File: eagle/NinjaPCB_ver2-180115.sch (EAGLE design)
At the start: 78 parts, among them IC2 VNH3SP30-BNC, IC3 ANALOGSW_AD_SOT23-6NC, IC4 ANALOGSW_TI-SC70-5/6NC, IC5 MCP3551SNNC, IC6 NAU7802NC, J2 ATX24, J3 HEATER, J4 HEATER_TEMP, J5 PELTIER, Q2 IRF520NPBF, Q3 IRF520NPBF, U1 CJT1117-3.3-SOT223

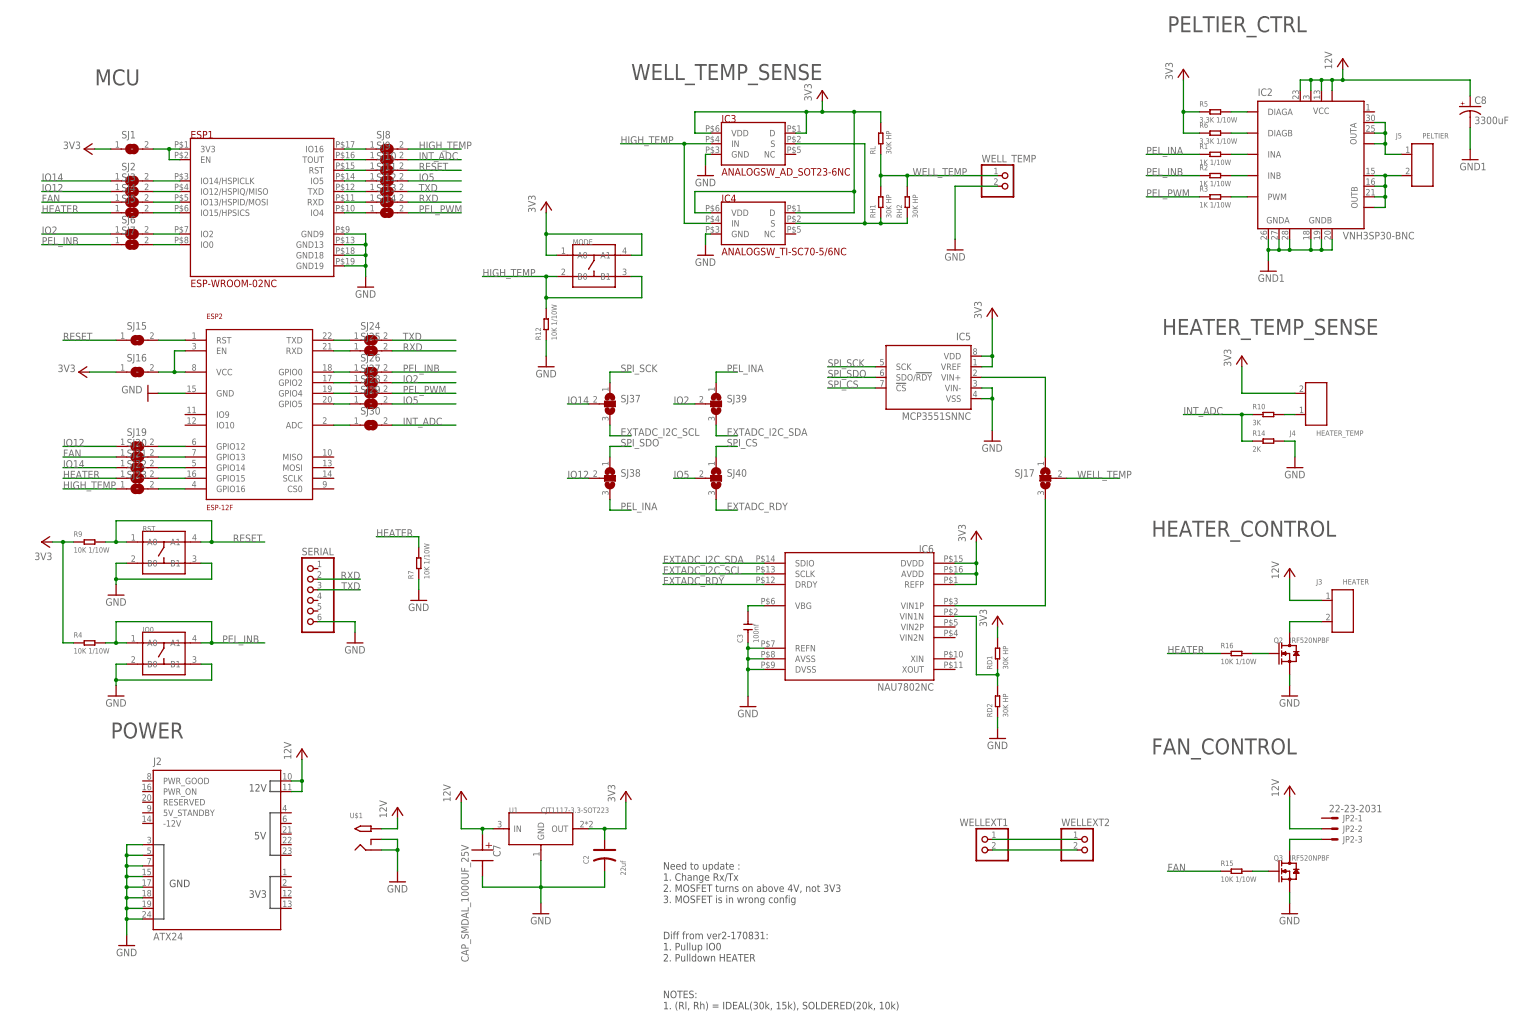
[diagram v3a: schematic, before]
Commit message: use relay instead of driver
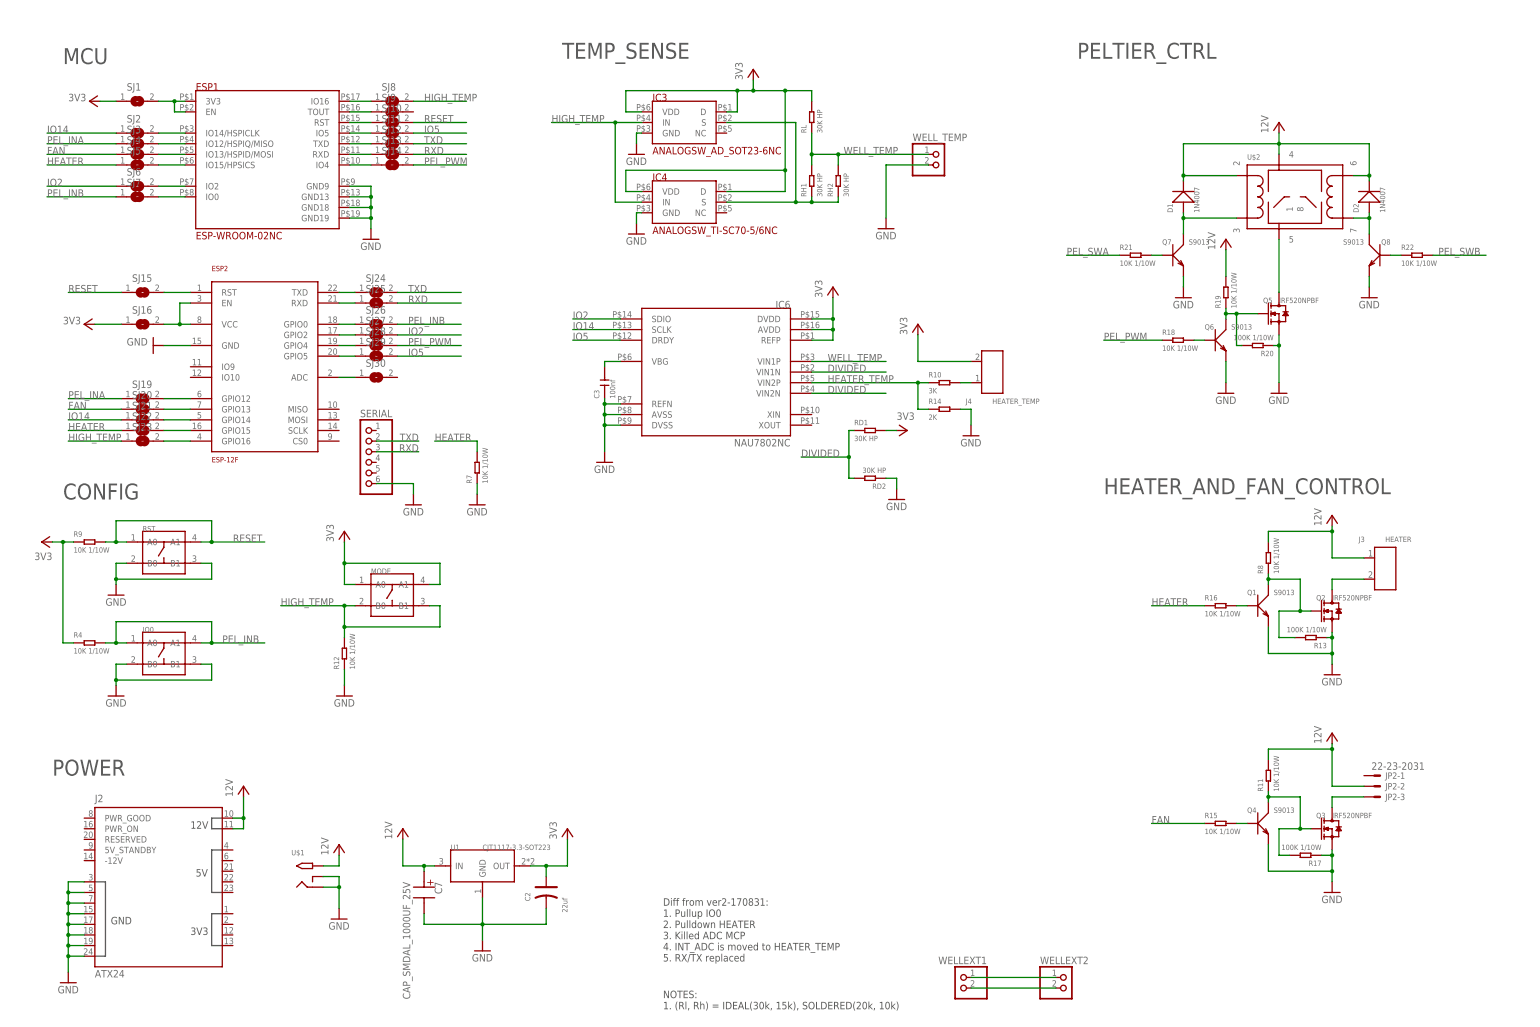
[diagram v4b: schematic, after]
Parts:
- removed C8: 3300uF, PCR-RCL:CAP_E5-13-L3030RINV
- removed IC2: VNH3SP30-BNC, st-microelectronics:VNH3SP30-BNC
- removed IC5: MCP3551SNNC, microchip:MCP3551SNNC
- removed J5: PELTIER, Seeed-Connector:SCREW-TERMINAL-GREEN(2P-3.5)
- removed R1, R2, R3: 1K 1/10W, Seeed-Resistor:SMD-RES-1K-5%-1/10W(0603)
- removed R5, R6: 3.3K 1/10W, Seeed-Resistor:SMD-RES-3.3K-5%-1/10W(0603)
- removed SJ17, SJ37, SJ38, SJ39, SJ40: (no value), jumper:SJ2W
- added D1, D2: 1N4007, Seeed-Diode:DIODE-GEN-PURPOSE-1KV-1A(DO-214AC)
- added Q1, Q4, Q6, Q7, Q8: S9013, Seeed-Transistor:SMD-TRANSISTORS-NPN-25V-500MA-S9013(SOT-23)
- added Q5: IRF520NPBF, Seeed-Transistor:DIP-MOSFET-N-CH-100V-9.7A-IRF520NPBF(TO-220AB)CORRECT
- added R11, R18, R19, R21, R22, R8: 10K 1/10W, Seeed-Resistor:SMD-RES-10K-5%-1/10W(0603)
- added R13, R17, R20: 100K 1/10W, Seeed-Resistor:SMD-RES-100K-5%-1/10W(0603)
- added U$2: NEC-RELAY2ET2, PCR-Switch:NEC-RELAY2ET2
- Q2, Q3: device Seeed-Transistor:DIP-MOSFET-N-CH-100V-9.7A-IRF520NPBF(TO-220AB) -> Seeed-Transistor:DIP-MOSFET-N-CH-100V-9.7A-IRF520NPBF(TO-220AB)CORRECT
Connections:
- removed net EXTADC_I2C_SCL: IC6.SCLK, SJ37.3
- removed net EXTADC_I2C_SDA: IC6.SDIO, SJ39.3
- removed net EXTADC_RDY: IC6.DRDY, SJ40.3
- removed net I2C_WELL_TEMP: IC6.VIN1P, SJ17.3
- removed net INT_ADC: R10.1, R14.1, SJ30.2, SJ9.2
- removed net IO12: SJ19.1, SJ3.1, SJ38.2
- removed net N$10: IC2.PWM, R3.2
- removed net N$6: IC2.DIAGA, R5.2
- removed net N$7: IC2.DIAGB, R6.2
- removed net N$8: IC2.INA, R1.2
- removed net N$9: IC2.INB, R2.2
- removed net N$91: IC6.VIN1N, RD1.1, RD2.2
- removed net OUTA: IC2.OUTA@1, IC2.OUTA@2, IC2.OUTA@3, J5.1
- removed net OUTB: IC2.OUTB, IC2.OUTB@1, IC2.OUTB@2, IC2.OUTB@3, J5.2
- removed net SPI_CS: IC5.!CS, SJ40.1
- removed net SPI_SCK: IC5.SCK, SJ37.1
- removed net SPI_SDO: IC5.SDO/!RDY, SJ38.1
- removed net SPI_WELL_TEMP: IC5.VIN+, SJ17.1
- new net DIVIDED: IC6.VIN1N, IC6.VIN2N, RD1.1, RD2.2
- new net HEATER_TEMP: IC6.VIN2P, R10.1, R14.1
- new net N$25: Q3.G, Q4.C, R11.1, R17.2
- new net N$29: Q1.C, Q2.G, R13.2, R8.1
- new net N$30: Q6.B, R18.2
- new net N$31: Q4.B, R15.2
- new net N$32: Q1.B, R16.2
- new net N$33: D1.+, Q7.C, U$2.3
- new net N$34: Q7.B, R21.2
- new net N$35: Q8.B, R22.1
- new net N$36: D2.+, Q8.C, U$2.7
- new net PEL_SWA: R21.1
- new net PEL_SWB: R22.2
- net 12V: now also D1.-, D2.-, R11.2, R19.2, R8.2, U$2.2, U$2.4, U$2.6; no longer C8.+, IC2.VCC, IC2.VCC@1, IC2.VCC@2, IC2.VCC@3
- net 3V3: no longer IC5.VDD, IC5.VREF, R5.1, R6.1
- net GND: now also Q1.E, Q4.E, Q5.S, Q6.E, Q7.E, Q8.E, R13.1, R17.1, R20.1; no longer C8.-, IC2.GNDA, IC2.GNDA@1, IC2.GNDA@2, IC2.GNDB, IC2.GNDB@1, IC2.GNDB@2, IC5.VIN-, IC5.VSS
- net HEATER: now also R7.2
- net IO14: now also IC6.SCLK; no longer SJ37.2
- net IO2: now also IC6.SDIO; no longer SJ39.2
- net IO5: now also IC6.DRDY; no longer SJ40.2
- net N$3: now also Q5.D, U$2.5; no longer Q2.G, R16.2
- net N$5: now also Q5.G, Q6.C, R19.1, R20.2; no longer Q3.G, R15.2
- net PEL_INA: now also SJ19.1, SJ3.1; no longer R1.1, SJ38.3, SJ39.1
- net PEL_INB: no longer R2.1
- net PEL_PWM: now also R18.1; no longer R3.1
- net RXD: now also SERIAL.3; no longer SERIAL.2
- net TXD: now also SERIAL.2; no longer SERIAL.3
- net WELL_TEMP: now also IC6.VIN1P; no longer SJ17.2
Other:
- note added: "CONFIG"
- note added: "Diff from ver2-170831: 1. Pullup IO0 2. Pulldown HEATER 3. Killed ADC MCP 4. INT_ADC is moved to HEATER_TEMP 5. RX/TX replaced"
- note added: "HEATER_AND_FAN_CONTROL"
- note added: "TEMP_SENSE"
- note removed: "Diff from ver2-170831: 1. Pullup IO0 2. Pulldown HEATER"
- note removed: "FAN_CONTROL"
- note removed: "HEATER_CONTROL"
- note removed: "HEATER_TEMP_SENSE"
- note removed: "Need to update : 1. Change Rx/Tx 2. MOSFET turns on above 4V, not 3V3 3. MOSFET is in wrong config"
- note removed: "WELL_TEMP_SENSE"
- moved on the sheet: C2, C3, C7, ESP1, ESP2, IC3, IC4, IC6, J2, J3, J4, JP2-1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

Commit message: add ESP-12F-breakout compatible with ESP-WROOM-02-breakout
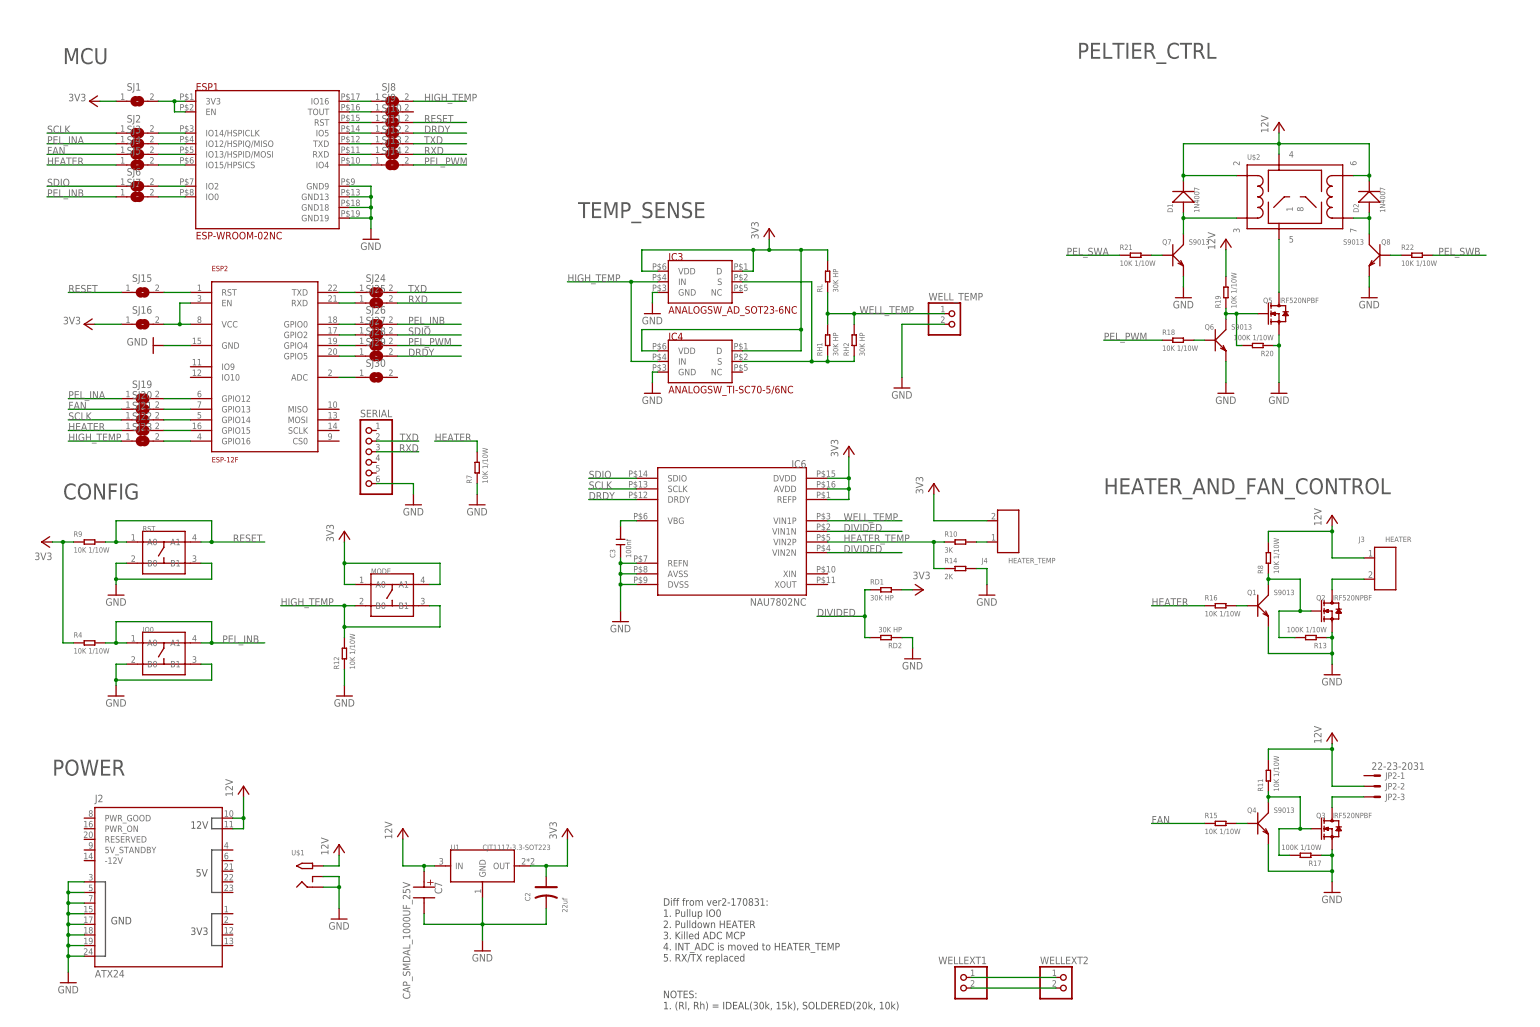
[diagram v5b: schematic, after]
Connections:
- net IO14 renamed SCLK
- net IO2 renamed SDIO
- net IO5 renamed DRDY
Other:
- moved on the sheet: C3, IC3, IC4, IC6, J4, R10, R14, RD1, RD2, RH1, RH2, RL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

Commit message: use breakout board
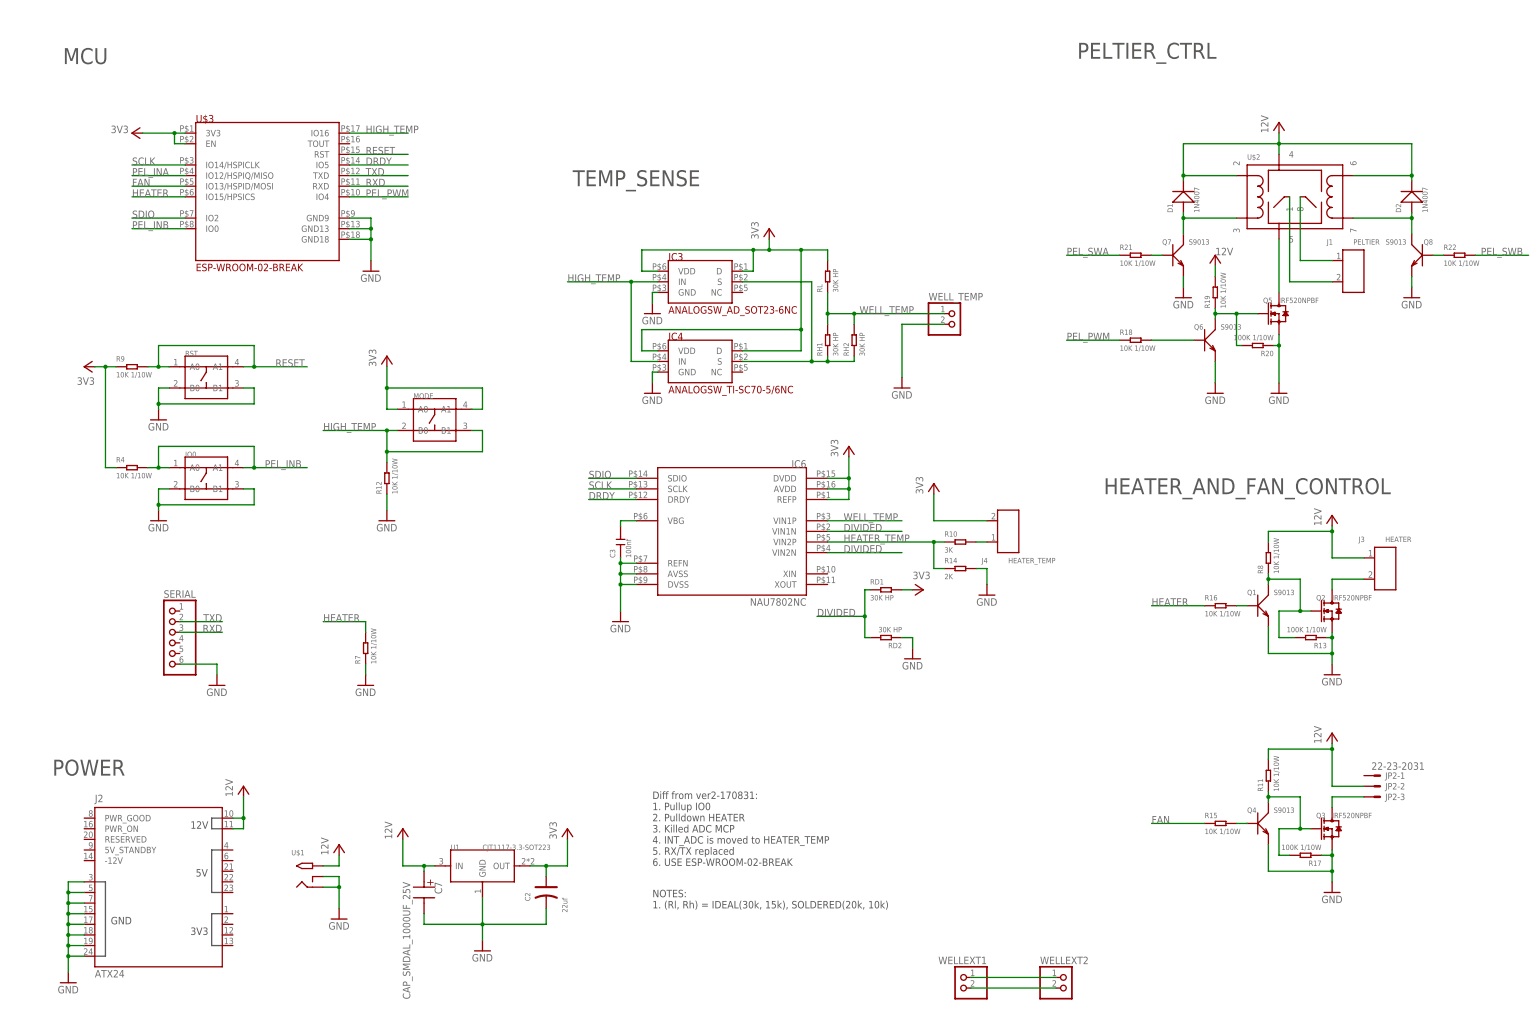
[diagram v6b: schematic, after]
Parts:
- removed ESP1: ESP-WROOM-02NC, PCR-Module:ESP-WROOM-02NC
- removed ESP2: ESP-12F, Seeed-OPL-2017-01-Sensor-camilo:ESP-12F
- removed SJ1, SJ10, SJ11, SJ12, SJ13, SJ14, SJ15, SJ16, SJ19, SJ2, SJ20, SJ21, SJ22, SJ23, SJ24, SJ25, SJ26, SJ27, SJ28, SJ29, SJ3, SJ30, SJ4, SJ5, SJ6, SJ7, SJ8, SJ9: (no value), jumper:SJ
- added J1: PELTIER, Seeed-Connector:SCREW-TERMINAL-GREEN(2P-3.5)
- added U$3: ESP-WROOM-02-BREAK, PCR-Module:ESP-WROOM-02-BREAK
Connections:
- removed net N$11: ESP1.3V3, ESP1.EN, SJ1.2
- removed net N$12: ESP1.IO14/HSPICLK, SJ2.2
- removed net N$13: ESP1.IO12/HSPIQ/MISO, SJ3.2
- removed net N$14: ESP1.IO13/HSPID/MOSI, SJ4.2
- removed net N$15: ESP1.IO15/HPSICS, SJ5.2
- removed net N$16: ESP1.IO2, SJ6.2
- removed net N$17: ESP1.IO0, SJ7.2
- removed net N$18: ESP1.IO16, SJ8.1
- removed net N$19: ESP1.TOUT, SJ9.1
- removed net N$20: ESP1.RST, SJ10.1
- removed net N$21: ESP1.IO5, SJ11.1
- removed net N$22: ESP1.TXD, SJ12.1
- removed net N$23: ESP1.RXD, SJ13.1
- removed net N$24: ESP1.IO4, SJ14.1
- removed net N$40: ESP2.RST, SJ15.2
- removed net N$42: ESP2.EN, ESP2.VCC, SJ16.2
- removed net N$43: ESP2.TXD, SJ24.1
- removed net N$44: ESP2.RXD, SJ25.1
- removed net N$45: ESP2.GPIO0, SJ26.1
- removed net N$46: ESP2.GPIO2, SJ27.1
- removed net N$47: ESP2.GPIO4, SJ28.1
- removed net N$48: ESP2.GPIO5, SJ29.1
- removed net N$49: ESP2.ADC, SJ30.1
- removed net N$67: ESP2.GPIO12, SJ19.2
- removed net N$68: ESP2.GPIO13, SJ20.2
- removed net N$69: ESP2.GPIO14, SJ21.2
- removed net N$70: ESP2.GPIO15, SJ22.2
- removed net N$71: ESP2.GPIO16, SJ23.2
- new net N$6: J1.1, U$2.8
- new net N$7: J1.2, U$2.1
- net 3V3: now also U$3.3V3, U$3.EN; no longer SJ1.1, SJ16.1
- net DRDY: now also U$3.IO5; no longer SJ11.2, SJ29.2
- net FAN: now also U$3.IO13/HSPID/MOSI; no longer SJ20.1, SJ4.1
- net GND: now also U$3.GND13, U$3.GND18, U$3.GND9; no longer ESP1.GND13, ESP1.GND18, ESP1.GND19, ESP1.GND9, ESP2.GND
- net HEATER: now also U$3.IO15/HPSICS; no longer SJ22.1, SJ5.1
- net HIGH_TEMP: now also U$3.IO16; no longer SJ23.1, SJ8.2
- net PEL_INA: now also U$3.IO12/HSPIQ/MISO; no longer SJ19.1, SJ3.1
- net PEL_INB: now also U$3.IO0; no longer SJ26.2, SJ7.1
- net PEL_PWM: now also U$3.IO4; no longer SJ14.2, SJ28.2
- net RESET: now also U$3.RST; no longer SJ10.2, SJ15.1
- net RXD: now also U$3.RXD; no longer SJ13.2, SJ25.2
- net SCLK: now also U$3.IO14/HSPICLK; no longer SJ2.1, SJ21.1
- net SDIO: now also U$3.IO2; no longer SJ27.2, SJ6.1
- net TXD: now also U$3.TXD; no longer SJ12.2, SJ24.2
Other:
- note added: "Diff from ver2-170831: 1. Pullup IO0 2. Pulldown HEATER 3. Killed ADC MCP 4. INT_ADC is moved to HEATER_TEMP 5. RX/TX replaced 6. USE ESP-WROOM-02-BREAK"
- note removed: "CONFIG"
- note removed: "Diff from ver2-170831: 1. Pullup IO0 2. Pulldown HEATER 3. Killed ADC MCP 4. INT_ADC is moved to HEATER_TEMP 5. RX/TX replaced"
- moved on the sheet: D2, IO0, MODE, Q6, Q8, R12, R18, R19, R22, R4, R7, R9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

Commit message: latest updates
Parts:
- removed U$3: ESP-WROOM-02-BREAK, PCR-Module:ESP-WROOM-02-BREAK
- added ESP1: ESP-12F, Seeed-OPL-2017-01-Sensor-camilo:ESP-12F
- added ESP2: ESP-WROOM-02-BREAK, PCR-Module:ESP-WROOM-02-BREAK
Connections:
- net 3V3: now also ESP1.EN, ESP1.VCC, ESP2.3V3, ESP2.EN; no longer U$3.3V3, U$3.EN
- net DRDY: now also ESP1.GPIO5, ESP2.IO5; no longer U$3.IO5
- net FAN: now also ESP1.GPIO13, ESP2.IO13/HSPID/MOSI; no longer U$3.IO13/HSPID/MOSI
- net GND: now also ESP1.GND, ESP2.GND13, ESP2.GND18, ESP2.GND9; no longer U$3.GND13, U$3.GND18, U$3.GND9
- net HEATER: now also ESP1.GPIO15, ESP2.IO15/HPSICS; no longer U$3.IO15/HPSICS
- net HIGH_TEMP: now also ESP1.GPIO16, ESP2.IO16; no longer U$3.IO16
- net PEL_INA: now also ESP1.GPIO12, ESP2.IO12/HSPIQ/MISO; no longer U$3.IO12/HSPIQ/MISO
- net PEL_INB: now also ESP1.GPIO0, ESP2.IO0; no longer U$3.IO0
- net PEL_PWM: now also ESP1.GPIO4, ESP2.IO4; no longer U$3.IO4
- net RESET: now also ESP1.RST, ESP2.RST; no longer U$3.RST
- net RXD: now also ESP1.RXD, ESP2.RXD; no longer U$3.RXD
- net SCLK: now also ESP1.GPIO14, ESP2.IO14/HSPICLK; no longer U$3.IO14/HSPICLK
- net SDIO: now also ESP1.GPIO2, ESP2.IO2; no longer U$3.IO2
- net TXD: now also ESP1.TXD, ESP2.TXD; no longer U$3.TXD
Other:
- moved on the sheet: C3, IC3, IC4, IC6, IO0, J4, MODE, R10, R12, R14, R4, R7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

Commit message: finished
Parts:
- removed IC4: ANALOGSW_TI-SC70-5/6NC, PCR-IC:ANALOGSW_TI-SC70-5/6NC
- removed J1: PELTIER, Seeed-Connector:SCREW-TERMINAL-GREEN(2P-3.5)
- removed WELLEXT1, WELLEXT2: (no value), pinhead:PINHD-1X2
- added PEL_BLK, PEL_RED: (no value), pinhead:PINHD-1X1L
- added PWR: (no value), pinhead:PINHD-1X2
- IC3: value ANALOGSW_AD_SOT23-6NC -> ANALOGSW_AD_SOT23-6; device PCR-IC:ANALOGSW_AD_SOT23-6NC -> PCR-IC:ANALOGSW_AD_SOT23-6
- IC6: value NAU7802NC -> NAU7802; device PCR-IC:NAU7802NC -> PCR-IC:NAU7802
- RD1, RD2, RH1, RH2, RL: device PCR-RCL:R0603NC -> PCR-RCL:R0603
- renumbered U$1 to JACK, U$2 to RELAY
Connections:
- removed net N$26: WELLEXT1.1, WELLEXT2.1
- removed net N$28: WELLEXT1.2, WELLEXT2.2
- removed net PEL_INA: ESP1.GPIO12, ESP2.IO12/HSPIQ/MISO
- removed net PEL_INB: ESP1.GPIO0, ESP2.IO0, IO0.A0, IO0.A1, R4.2
- new net PWR: PWR.1, SERIAL.4
- net 3V3: now also J4.1, PWR.2; no longer IC4.D, IC4.VDD, J4.2
- net GND: no longer IC4.GND
- net HIGH_TEMP: no longer IC4.IN
- net N$1: now also J4.2; no longer J4.1
- net N$27: no longer IC4.S
- net N$6: now also PEL_RED.1; no longer J1.1
- net N$7: now also PEL_BLK.1; no longer J1.2
- net PEL_SWA: now also ESP1.GPIO12, ESP2.IO12/HSPIQ/MISO
- net PEL_SWB: now also ESP1.GPIO0, ESP2.IO0, IO0.A0, IO0.A1, R4.2
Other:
- moved on the sheet: J4, RH1, RH2, RL, WELL_TEMP
